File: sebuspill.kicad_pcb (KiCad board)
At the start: 2 copper layers, 26 parts, among them J1 Conn_01x04_Male, J3 Pinout 1, J4 Pinout 2, SW1 SW_SPDT, U1 AMS1117-3.3, U2 STM32F103C8T6, Y1 16MHz

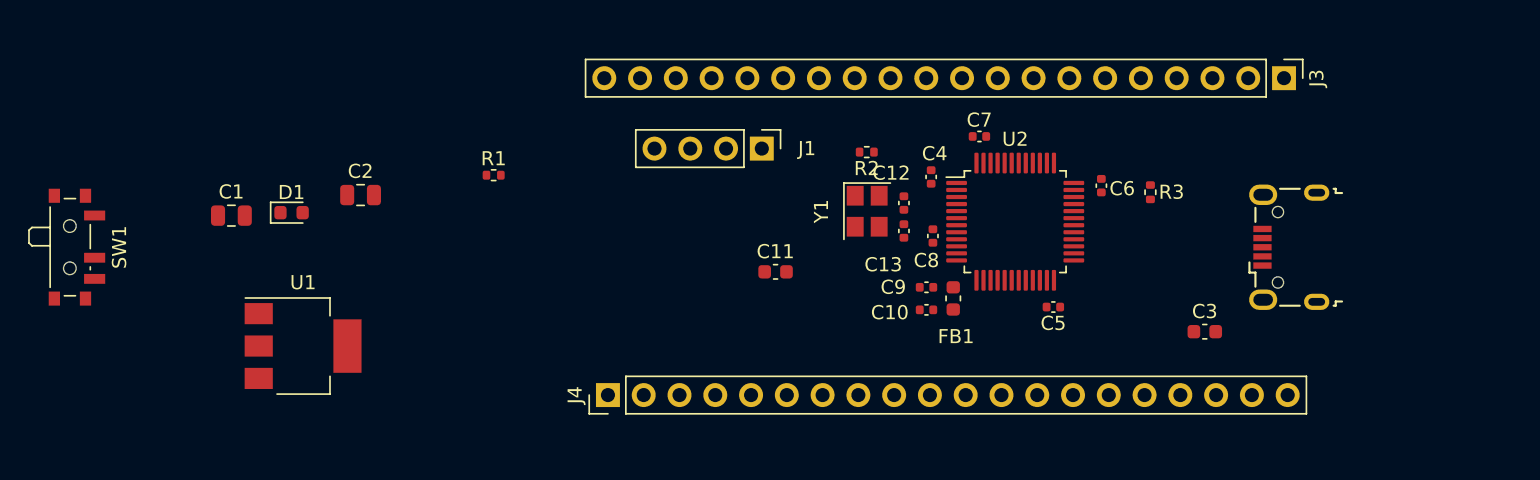
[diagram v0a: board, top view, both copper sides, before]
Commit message: added all components, next step routing and outline
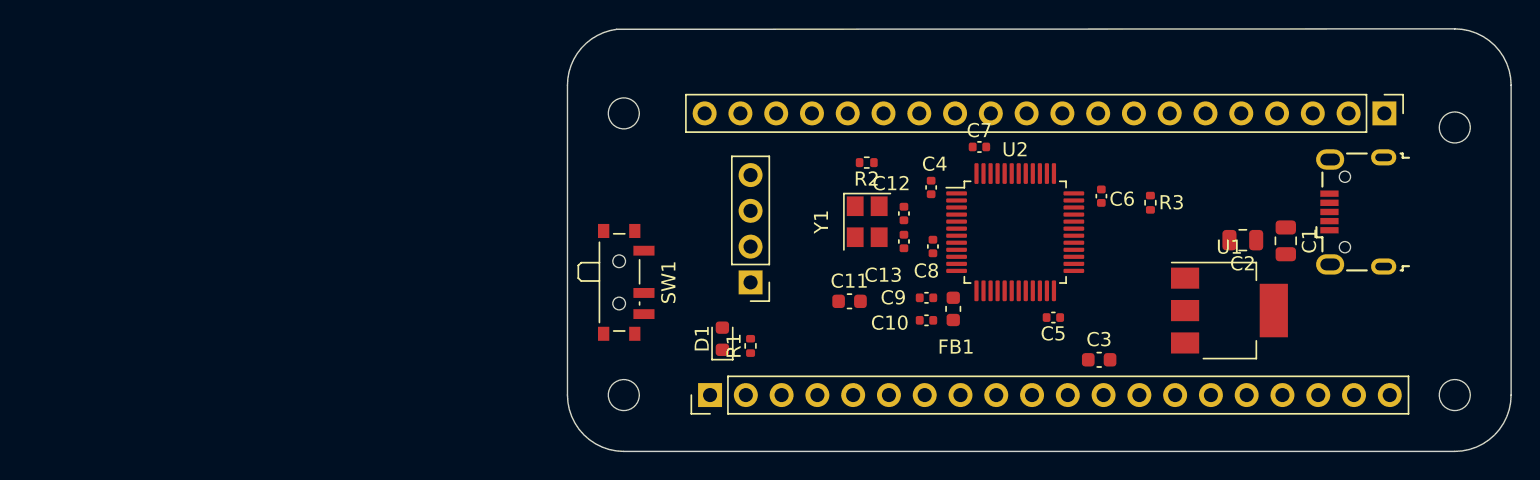
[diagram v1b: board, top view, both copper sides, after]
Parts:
- added H1: MountingHole, MountingHole:MountingHole_2.2mm_M2, F.Cu at (134.0, 94.0)
- added H2: MountingHole, MountingHole:MountingHole_2.2mm_M2, F.Cu at (193.0, 114.0)
- added H3: MountingHole, MountingHole:MountingHole_2.2mm_M2, F.Cu at (134.0, 114.0)
- added H4: MountingHole, MountingHole:MountingHole_2.2mm_M2, F.Cu at (193.0, 95.0)
- J2: renamed from  
- moved C1 74.9 mm to (181.0, 103.0), turned to -90 degrees
- moved U1 65.8 mm to (177.0, 108.0)
- moved C2 62.7 mm to (177.9, 103.0), turned to 180 degrees
- moved SW1 39.1 mm to (134.0, 106.0)
- moved D1 31.9 mm to (141.0, 110.0), turned to 90 degrees
- moved R1 21.9 mm to (143.0, 110.5), turned to 90 degrees
- moved J1 9.53 mm to (143.0, 106.0), turned to 180 degrees
- moved C3 7.76 mm to (167.8, 111.5)
- moved J3 7.55 mm to (188.0, 94.0)
- moved J4 7.25 mm to (140.1, 114.0)
- moved C11 5.65 mm to (150.0, 107.3)
- moved J2 5.37 mm to (186.0, 101.0)
- moved C10 0.75 mm to (155.5, 108.7)
- moved C12 0.75 mm to (153.9, 101.1)
- moved C13 0.75 mm to (153.9, 103.1)
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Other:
- board outline added: 67 x 30 mm

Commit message: set pinheaders to fit on a bread board
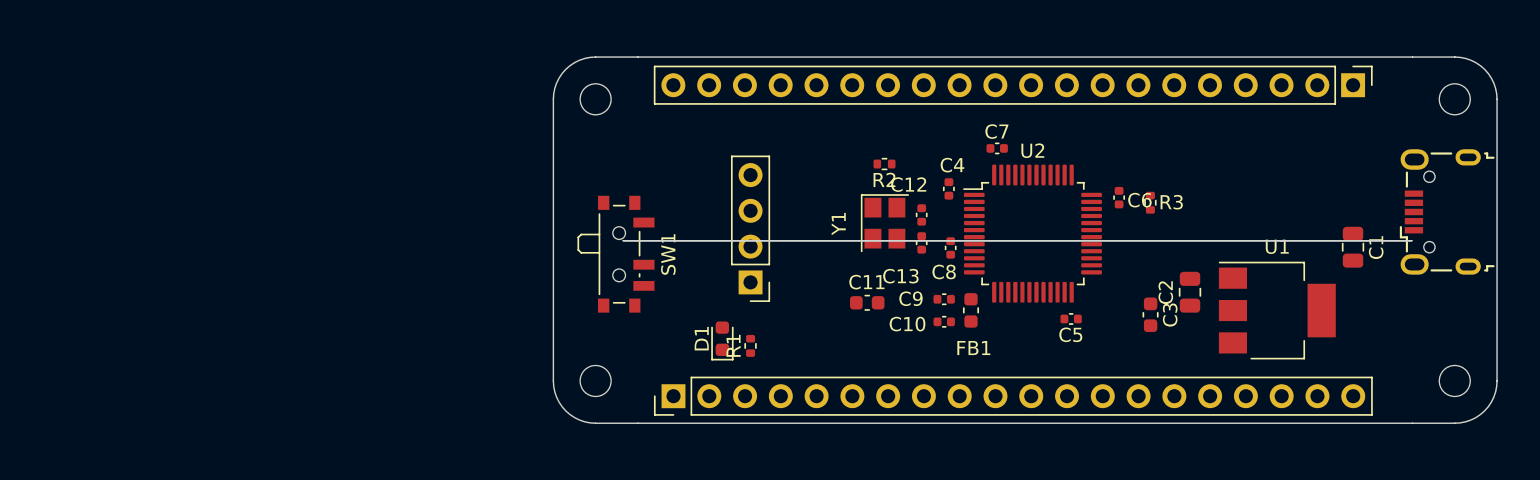
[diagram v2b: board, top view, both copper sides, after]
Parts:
- moved H3 21.1 mm to (132.0, 93.0)
- moved H2 21.0 mm to (193.0, 93.0)
- moved H1 19.1 mm to (132.0, 113.0)
- moved H4 18.0 mm to (193.0, 113.0)
- moved J2 6.00 mm to (192.0, 101.0)
- moved C2 5.27 mm to (174.2, 106.7), turned to 90 degrees
- moved C3 4.85 mm to (171.4, 108.3), turned to -90 degrees
- moved C1 4.80 mm to (185.8, 103.5)
- moved U1 3.40 mm to (180.4, 108.0)
- moved J3 2.99 mm to (185.8, 92.0)
- moved J4 2.60 mm to (137.5, 114.1)
- moved SW1 2.00 mm to (134.0, 104.0)
- moved C12 1.26 mm to (155.2, 101.2)
- moved C13 1.26 mm to (155.2, 103.2)
- moved C6 1.26 mm to (169.2, 100.0)
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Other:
- board size 67 x 30 mm -> 67 x 26 mm

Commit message: routing halfly done
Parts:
- moved D1 46.8 mm to (187.8, 109.8), turned to 180 degrees
- moved R1 45.0 mm to (188.0, 108.5), turned to 180 degrees
- moved C11 8.18 mm to (143.2, 108.8), turned to 180 degrees
- moved R3 7.78 mm to (179.2, 100.7)
- moved SW1 3.55 mm to (131.7, 101.3)
- moved C1 1.90 mm to (187.0, 105.0)
- moved C3 1.76 mm to (169.6, 108.3), turned to 90 degrees
- moved FB1 1.55 mm to (157.1, 108.0)
- moved C10 1.55 mm to (155.2, 108.8)
- moved C9 1.55 mm to (155.2, 107.2)
- moved C8 1.50 mm to (156.2, 104.6), turned to 45 degrees
- moved J2 0.44 mm to (191.6, 101.2)
- moved C5 0.40 mm to (166.2, 108.6)
- moved C6 0.33 mm to (169.2, 99.7)
- moved C7 0.29 mm to (160.2, 96.6)
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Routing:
- net +3V3: track 0.00 -> 144.3 mm
- net GND: track 0.00 -> 37.4 mm, vias 0 -> 14
- net /SWDIO: track 0.00 -> 27.6 mm, vias 0 -> 4
- net PC15: track 0.00 -> 26.3 mm
- net /USB_D+: track 0.00 -> 22.6 mm
- net /USB_D-: track 0.00 -> 22.6 mm
- net /BOOTP_SW: track 0.00 -> 21.6 mm
- net PA0: track 0.00 -> 21.5 mm, vias 0 -> 2
- net PB9: track 0.00 -> 21.2 mm
- net VBUS: track 0.00 -> 19.3 mm
- net PB8: track 0.00 -> 19.3 mm
- net /NRST: track 0.00 -> 18.6 mm, vias 0 -> 4
- net PB7: track 0.00 -> 17.5 mm
- net PB11: track 0.00 -> 15.8 mm
- net PA1: track 0.00 -> 15.7 mm
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- added copper zone on B.Cu, net GND
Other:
- outline, holes or cut-outs redrawn

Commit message: still routing
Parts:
- moved R2 0.98 mm to (153.1, 96.8)
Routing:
- net /SWCLK: track 0.00 -> 27.1 mm, vias 0 -> 2
- net GND: track 37.4 -> 40.4 mm, vias 14 -> 15
- net PA15: track 6.69 -> 8.43 mm
- net PB3: track 10.1 -> 10.3 mm, vias 0 -> 2
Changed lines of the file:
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@@
   )
   (footprint "Resistor_SMD:R_0402_1005Metric" (layer "F.Cu")
-    (at 152.510046 97.59811 180)
+    (at 153.128 96.836 180)
     (descr "Resistor SMD 0402 (1005 Metric), square (rectangular) end terminal, IPC_7351 nominal, (Body size source: IPC-SM-782 page 72, https://www.pcb-3d.com/wordpress/wp-content/uploads/ipc-sm-782a_amendment_1_and_2.pdf), generated with kicad-footprint-generator")
     (tags "resistor")
@@
   (segment (start 153.985 107.9725) (end 153.855 108.1025) (width 0.3) (layer "F.Cu") (net 2))
   (segment (start 165.68 108.59) (end 165.68 109.25) (width 0.3) (layer "F.Cu") (net 2))
+  (segment (start 140.664 98.38) (end 140.176 98.868) (width 0.3) (layer "F.Cu") (net 2))
   (segment (start 165.68 109.25) (end 165.94 109.51) (width 0.3) (layer "F.Cu") (net 2))
   (segment (start 154.725 107.9725) (end 153.985 107.9725) (width 0.3) (layer "F.Cu") (net 2))
@@
   (segment (start 156.016355 98.766355) (end 156 98.75) (width 0.3) (layer "F.Cu") (net 2))
   (segment (start 156.25 98.75) (end 156.266355 98.766355) (width 0.3) (layer "F.Cu") (net 2))
+  (segment (start 143 98.38) (end 140.664 98.38) (width 0.3) (layer "F.Cu") (net 2))
   (segment (start 160.8 96.68) (end 160.72 96.6) (width 0.3) (layer "F.Cu") (net 2))
   (segment (start 170.765 107.525) (end 170.81 107.48) (width 0.3) (layer "F.Cu") (net 2))
@@
   (via (at 141.29 108.91) (size 0.8) (drill 0.4) (layers "F.Cu" "B.Cu") (net 2))
   (via (at 187.94 99.95) (size 0.8) (drill 0.4) (layers "F.Cu" "B.Cu") (net 2))
+  (via (at 140.176 98.868) (size 0.8) (drill 0.4) (layers "F.Cu" "B.Cu") (net 2))
   (via (at 154.69 99.66) (size 0.8) (drill 0.4) (layers "F.Cu" "B.Cu") (net 2))
   (via (at 156 98.75) (size 0.8) (drill 0.4) (layers "F.Cu" "B.Cu") (net 2))
@@
   (segment (start 188.5875 109.5475) (end 187.49 108.45) (width 0.3) (layer "F.Cu") (net 8))
   (segment (start 188.5875 109.85) (end 188.5875 109.5475) (width 0.3) (layer "F.Cu") (net 8))
-  (segment (start 166.373959 100.7875) (end 162.211459 104.95) (width 0.3) (layer "F.Cu") (net 9))
   (segment (start 155.53 106.2) (end 149.53 106.2) (width 0.3) (layer "F.Cu") (net 9))
   (segment (start 167.2125 100.7875) (end 166.373959 100.7875) (width 0.3) (layer "F.Cu") (net 9))
@@
   (segment (start 162.211459 104.95) (end 160.84 104.95) (width 0.3) (layer "F.Cu") (net 9))
   (segment (start 145.71 106.17) (end 143 103.46) (width 0.3) (layer "F.Cu") (net 9))
+  (segment (start 166.373959 100.7875) (end 162.211459 104.95) (width 0.3) (layer "F.Cu") (net 9))
   (segment (start 147.98 106.17) (end 145.71 106.17) (width 0.3) (layer "F.Cu") (net 9))
   (via (at 147.98 106.17) (size 0.8) (drill 0.4) (layers "F.Cu" "B.Cu") (net 9))
@@
   (segment (start 149.52 106.19) (end 148 106.19) (width 0.3) (layer "B.Cu") (net 9))
   (segment (start 160.84 104.95) (end 159.59 106.2) (width 0.3) (layer "B.Cu") (net 9))
+  (segment (start 158.21 98.868) (end 158.21 98.614) (width 0.3) (layer "F.Cu") (net 10))
+  (segment (start 157.448 97.852) (end 146.068 97.852) (width 0.3) (layer "F.Cu") (net 10))
+  (segment (start 165.8 98.375) (end 165.8 99.213541) (width 0.3) (layer "F.Cu") (net 10))
+  (segment (start 164.875541 100.138) (end 161.004 100.138) (width 0.3) (layer "F.Cu") (net 10))
+  (segment (start 161.004 100.138) (end 161.004 100.285959) (width 0.3) (layer "F.Cu") (net 10))
+  (segment (start 165.8 98.375) (end 165.8 97.882) (width 0.3) (layer "F.Cu") (net 10))
+  (segment (start 165.8 99.213541) (end 164.875541 100.138) (width 0.3) (layer "F.Cu") (net 10))
+  (segment (start 158.21 98.614) (end 157.448 97.852) (width 0.3) (layer "F.Cu") (net 10))
+  (segment (start 146.068 97.852) (end 143 100.92) (width 0.3) (layer "F.Cu") (net 10))
+  (via (at 158.21 98.868) (size 0.8) (drill 0.4) (layers "F.Cu" "B.Cu") (net 10))
+  (via (at 161.004 100.285959) (size 0.8) (drill 0.4) (layers "F.Cu" "B.Cu") (net 10))
+  (segment (start 159.586041 98.868) (end 158.21 98.868) (width 0.3) (layer "B.Cu") (net 10))
+  (segment (start 161.004 100.285959) (end 159.586041 98.868) (width 0.3) (layer "B.Cu") (net 10))
   (segment (start 189.620677 101.7875) (end 189.730321 101.897144) (width 0.2) (layer "F.Cu") (net 11))
   (segment (start 167.2125 101.7875) (end 189.620677 101.7875) (width 0.2) (layer "F.Cu") (net 11))
@@
   (segment (start 189.639966 101.337499) (end 189.730321 101.247144) (width 0.2) (layer "F.Cu") (net 12))
   (segment (start 162.92 92) (end 162.92 92.148) (width 0.3) (layer "F.Cu") (net 24))
-  (segment (start 163.570908 92.798908) (end 164.279092 92.798908) (width 0.3) (layer "F.Cu") (net 24))
-  (segment (start 165.3 97.536459) (end 165.372501 97.463958) (width 0.3) (layer "F.Cu") (net 24))
-  (segment (start 165.372501 97.463958) (end 165.372501 93.531141) (width 0.3) (layer "F.Cu") (net 24))
-  (segment (start 162.92 92.148) (end 163.570908 92.798908) (width 0.3) (layer "F.Cu") (net 24))
-  (segment (start 165.3 97.536459) (end 165.3 98.375) (width 0.3) (layer "F.Cu") (net 24))
-  (segment (start 164.279092 92.798908) (end 164.306 92.772) (width 0.3) (layer "F.Cu") (net 24))
-  (segment (start 164.8 98.375) (end 164.8 94.43207) (width 0.3) (layer "F.Cu") (net 25))
-  (segment (start 162.509092 93.298908) (end 164.433162 93.298908) (width 0.3) (layer "F.Cu") (net 25))
-  (segment (start 164.8 94.43207) (end 164.872501 94.359569) (width 0.3) (layer "F.Cu") (net 25))
-  (segment (start 164.872501 93.738247) (end 164.872501 94.359569) (width 0.3) (layer "F.Cu") (net 25))
-  (segment (start 161.914 93.534) (end 160.38 92) (width 0.3) (layer "F.Cu") (net 25))
-  (segment (start 162.509092 93.298908) (end 162.274 93.534) (width 0.3) (layer "F.Cu") (net 25))
+  (segment (start 165.818 94.055057) (end 164.674471 92.911528) (width 0.3) (layer "F.Cu") (net 24))
+  (segment (start 165.3 98.375) (end 165.3 97.536459) (width 0.3) (layer "F.Cu") (net 24))
+  (segment (start 163.831528 92.911528) (end 162.92 92) (width 0.3) (layer "F.Cu") (net 24))
+  (segment (start 164.674471 92.911528) (end 163.831528 92.911528) (width 0.3) (layer "F.Cu") (net 24))
+  (segment (start 165.818 97.018459) (end 165.818 94.055057) (width 0.3) (layer "F.Cu") (net 24))
+  (segment (start 165.3 97.536459) (end 165.818 97.018459) (width 0.3) (layer "F.Cu") (net 24))
+  (segment (start 164.8 95.072) (end 164.8 98.375) (width 0.3) (layer "F.Cu") (net 25))
+  (segment (start 161.512 92.772) (end 162.02 93.28) (width 0.3) (layer "F.Cu") (net 25))
+  (segment (start 160.74 92) (end 161.512 92.772) (width 0.3) (layer "F.Cu") (net 25))
+  (segment (start 160.38 92) (end 160.74 92) (width 0.3) (layer "F.Cu") (net 25))
+  (segment (start 165.068 94.804) (end 164.8 95.072) (width 0.3) (layer "F.Cu") (net 25))
   (segment (start 160.38 92) (end 160.38 92.030915) (width 0.3) (layer "F.Cu") (net 25))
-  (segment (start 162.274 93.534) (end 161.914 93.534) (width 0.3) (layer "F.Cu") (net 25))
-  (segment (start 164.433162 93.298908) (end 164.872501 93.738247) (width 0.3) (layer "F.Cu") (net 25))
+  (via (at 165.068 94.804) (size 0.8) (drill 0.4) (layers "F.Cu" "B.Cu") (net 25))
+  (via (at 162.02 93.28) (size 0.8) (drill 0.4) (layers "F.Cu" "B.Cu") (net 25))
+  (segment (start 165.068 94.804) (end 165.068 93.933746) (width 0.3) (layer "B.Cu") (net 25))
+  (segment (start 165.068 93.933746) (end 164.414254 93.28) (width 0.3) (layer "B.Cu") (net 25))
+  (segment (start 164.872501 94.608501) (end 165.068 94.804) (width 0.3) (layer "B.Cu") (net 25))
+  (segment (start 164.414254 93.28) (end 162.02 93.28) (width 0.3) (layer "B.Cu") (net 25))
   (segment (start 164.3 98.375) (end 164.3 94.890961) (width 0.3) (layer "F.Cu") (net 26))
   (segment (start 157.84 93.150569) (end 158.092632 93.403201) (width 0.3) (layer "F.Cu") (net 26))
@@
   (segment (start 165.177106 110.4) (end 167.78 110.4) (width 0.3) (layer "F.Cu") (net 46))
   (segment (start 171.817057 111.11) (end 174.787057 114.08) (width 0.3) (layer "F.Cu") (net 46))
-  (segment (start 159.986459 99.536459) (end 158.04811 97.59811) (width 0.3) (layer "F.Cu") (net 48))
-  (segment (start 161.977082 99.536459) (end 159.986459 99.536459) (width 0.3) (layer "F.Cu") (net 48))
-  (segment (start 162.3 98.375) (end 162.3 99.213541) (width 0.3) (layer "F.Cu") (net 48))
-  (segment (start 162.3 99.213541) (end 161.977082 99.536459) (width 0.3) (layer "F.Cu") (net 48))
-  (segment (start 158.04811 97.59811) (end 153.020046 97.59811) (width 0.3) (layer "F.Cu") (net 48))
-  (segment (start 140.68 96.57) (end 135.206449 102.043551) (width 0.3) (layer "F.Cu") (net 49))
-  (segment (start 150.971936 96.57) (end 140.68 96.57) (width 0.3) (layer "F.Cu") (net 49))
-  (segment (start 135.206449 102.043551) (end 133.133299 102.043551) (width 0.3) (layer "F.Cu") (net 49))
-  (segment (start 152.000046 97.59811) (end 150.971936 96.57) (width 0.3) (layer "F.Cu") (net 49))
+  (segment (start 159.986459 99.536459) (end 161.977082 99.536459) (width 0.3) (layer "F.Cu") (net 48))
+  (segment (start 157.286 96.836) (end 159.986459 99.536459) (width 0.3) (layer "F.Cu") (net 48))
+  (segment (start 161.977082 99.536459) (end 162.3 99.213541) (width 0.3) (layer "F.Cu") (net 48))
+  (segment (start 153.638 96.836) (end 157.286 96.836) (width 0.3) (layer "F.Cu") (net 48))
+  (segment (start 162.3 99.213541) (end 162.3 98.375) (width 0.3) (layer "F.Cu") (net 48))
+  (segment (start 133.133299 102.043551) (end 135.206449 102.043551) (width 0.3) (layer "F.Cu") (net 49))
+  (segment (start 150.971936 96.57) (end 151.237936 96.836) (width 0.3) (layer "F.Cu") (net 49))
+  (segment (start 151.237936 96.836) (end 152.618 96.836) (width 0.3) (layer "F.Cu") (net 49))
+  (segment (start 140.68 96.57) (end 150.971936 96.57) (width 0.3) (layer "F.Cu") (net 49))
+  (segment (start 135.206449 102.043551) (end 140.68 96.57) (width 0.3) (layer "F.Cu") (net 49))
   (zone (net 2) (net_name "GND") (layer "B.Cu") (hatch edge 0.508)
     (connect_pads (clearance 0.3))

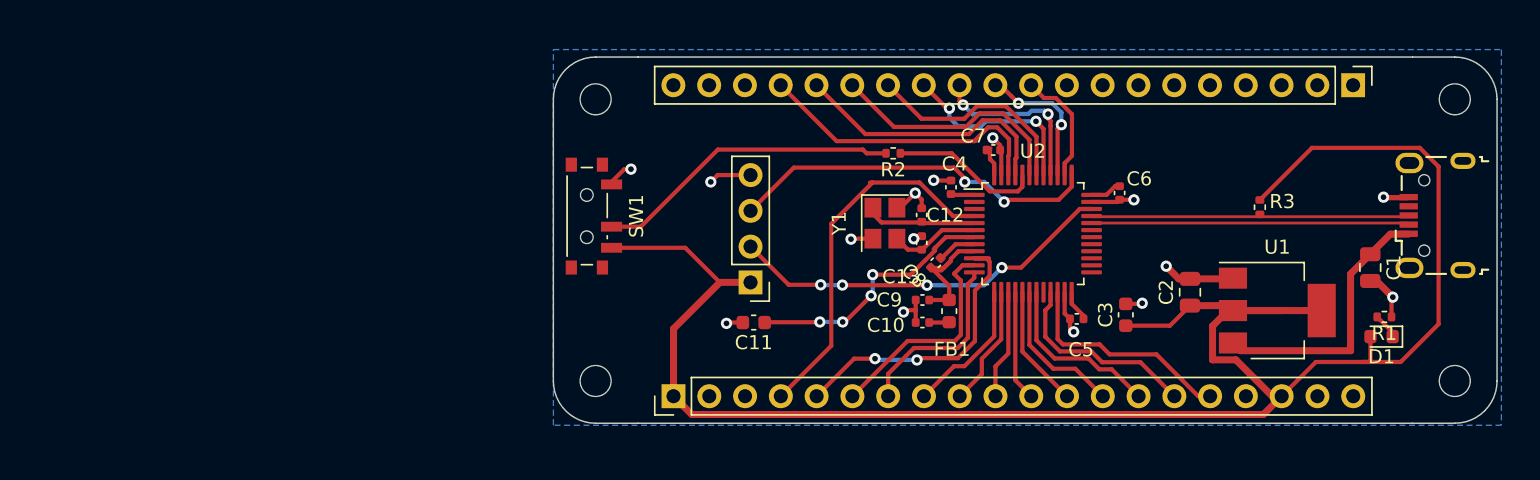
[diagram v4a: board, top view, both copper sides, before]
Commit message: trying to route groundplane between all backside wires
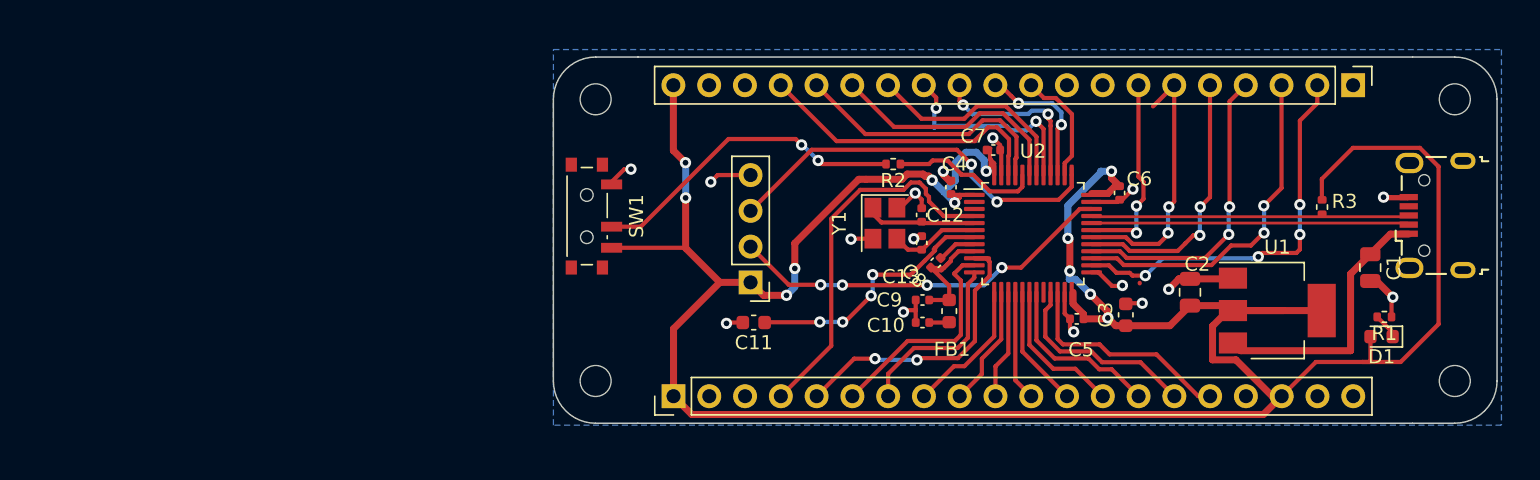
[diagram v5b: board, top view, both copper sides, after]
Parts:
- moved R3 4.42 mm to (183.6, 100.7)
- moved R2 0.76 mm to (153.1, 97.6)
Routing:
- net +3V3: track 144.3 -> 200.6 mm, vias 0 -> 12
- net PB13: track 0.00 -> 28.1 mm, vias 0 -> 4
- net PB14: track 0.00 -> 24.5 mm, vias 0 -> 2
- net PB15: track 0.00 -> 21.7 mm, vias 0 -> 2
- net PA8: track 0.00 -> 19.3 mm, vias 0 -> 2
- net PA9: track 0.00 -> 18.8 mm, vias 0 -> 2
- net PA10: track 0.00 -> 14.1 mm, vias 0 -> 2
- net PB12: track 0.00 -> 2.81 mm, vias 0 -> 1
- net /SWCLK: track 27.1 -> 28.4 mm
- net PB5: track 13.8 -> 15.1 mm
- net /BOOTP_SW: track 21.9 -> 22.8 mm, vias 0 -> 2
- net GND: track 40.4 -> 41.0 mm
